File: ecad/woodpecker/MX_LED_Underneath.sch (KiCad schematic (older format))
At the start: 6 parts, among them SW1 Cherry_MX_LED, U1 TLC5973

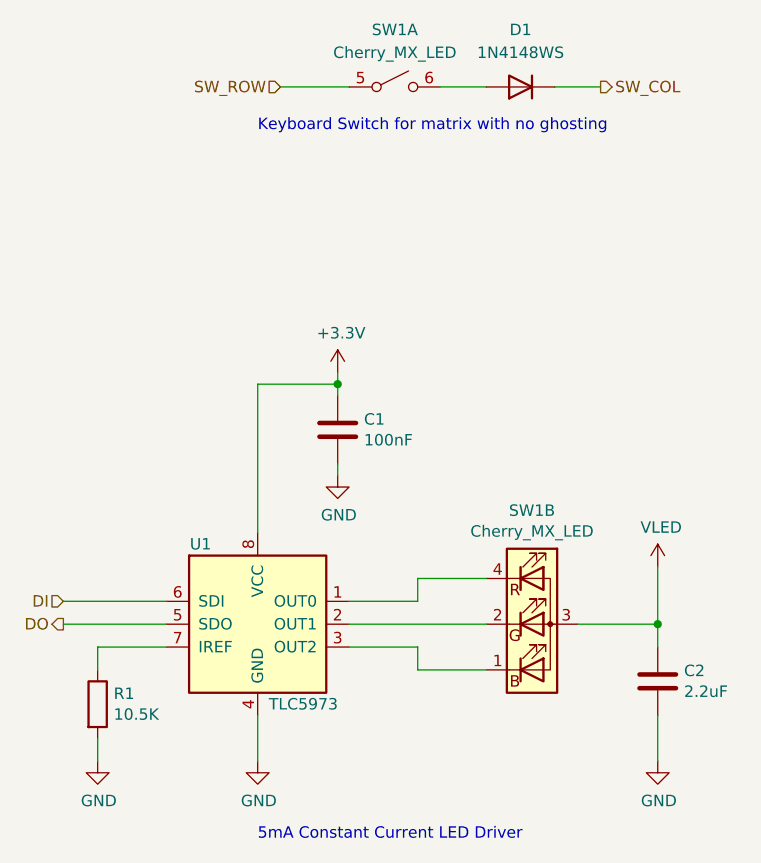
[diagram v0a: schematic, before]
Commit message: Adds bottom section in monolithic design
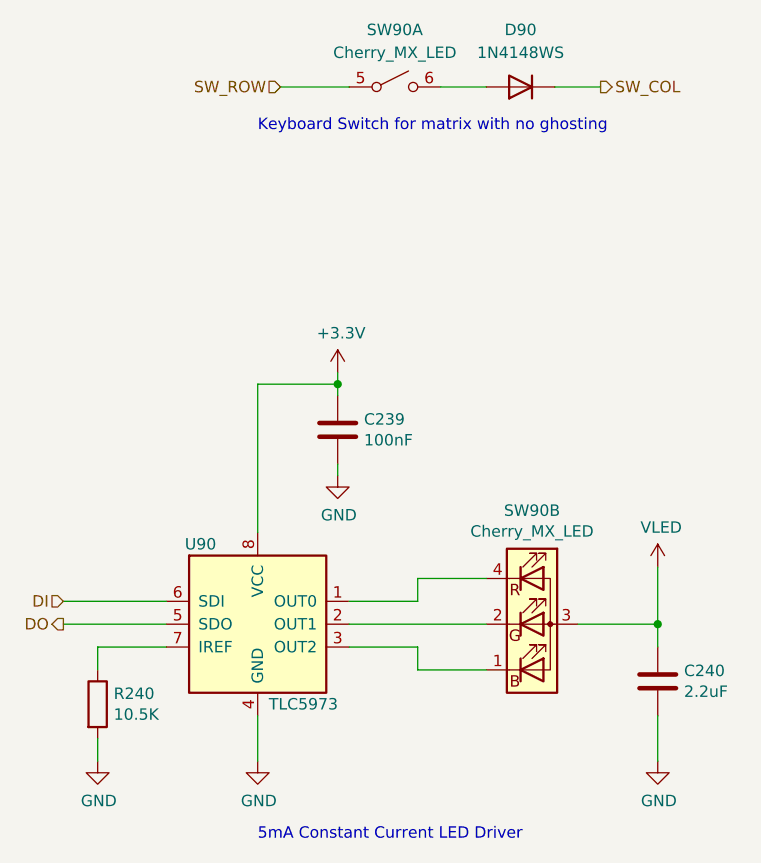
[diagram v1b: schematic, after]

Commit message: Corrects Quadrature encoder debounce circuit on put them on the scan matrix
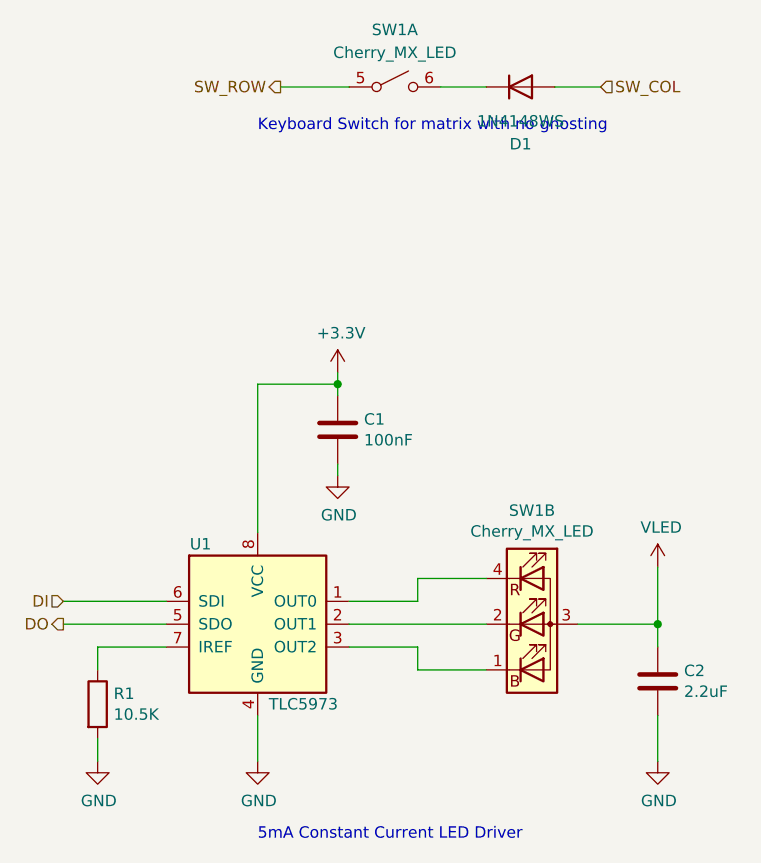
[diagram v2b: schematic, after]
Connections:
- net SW_COL: now also D1.2 (A); no longer D1.1 (K)
- net at SW1.6 (SW_B): now also D1.1 (K); no longer D1.2 (A)
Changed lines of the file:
@@
 $Descr A4 11693 8268
 encoding utf-8
-Sheet 81 97
+Sheet 3 97
 Title ""
 Date ""
@@
 AR Path="/60B694C9/60B3E46F/604B48F1" Ref="SW89"  Part="1"
 AR Path="/60B694C9/60B3E4B2/604B48F1" Ref="SW90"  Part="1"
-F 0 "SW90" H 5700 2950 50  0000 C CNN
+F 0 "SW1" H 5700 2950 50  0000 C CNN
 F 1 "Cherry_MX_LED" H 5700 2850 50  0000 C CNN
 F 2 "woodpecker:SW_Cherry_MX_1.00u_PCB_SMD_LED" H 5700 2700 50  0001 C CNN
@@
 AR Path="/60B694C9/60B3E46F/604B519A" Ref="SW89"  Part="2"
 AR Path="/60B694C9/60B3E4B2/604B519A" Ref="SW90"  Part="2"
-F 0 "SW90" H 6300 5547 50  0000 C CNN
+F 0 "SW1" H 6300 5547 50  0000 C CNN
 F 1 "Cherry_MX_LED" H 6300 5456 50  0000 C CNN
 F 2 "woodpecker:SW_Cherry_MX_1.00u_PCB_SMD_LED" H 6300 5050 50  0001 C CNN
@@
 AR Path="/60B694C9/60B3E46F/604B51B1" Ref="U89"  Part="1"
 AR Path="/60B694C9/60B3E4B2/604B51B1" Ref="U90"  Part="1"
-F 0 "U90" H 4850 5400 50  0000 C CNN
+F 0 "U1" H 4850 5400 50  0000 C CNN
 F 1 "TLC5973" H 5300 4700 50  0000 C CNN
 F 2 "Package_SO:SOIC-8_3.9x4.9mm_P1.27mm" H 5550 5400 50  0001 L CNN
@@
 AR Path="/60B694C9/60B3E46F/604BE188" Ref="C238"  Part="1"
 AR Path="/60B694C9/60B3E4B2/604BE188" Ref="C240"  Part="1"
-F 0 "C240" H 6965 5346 50  0000 L CNN
+F 0 "C2" H 6965 5346 50  0000 L CNN
 F 1 "2.2uF" H 6965 5255 50  0000 L CNN
 F 2 "Capacitor_SMD:C_0805_2012Metric_Pad1.18x1.45mm_HandSolder" H 6888 5150 50  0001 C CNN
@@
 AR Path="/60B694C9/60B3E46F/604BF391" Ref="#PWR0649"  Part="1"
 AR Path="/60B694C9/60B3E4B2/604BF391" Ref="#PWR0655"  Part="1"
-F 0 "#PWR0655" H 6850 5400 50  0001 C CNN
+F 0 "#PWR06" H 6850 5400 50  0001 C CNN
 F 1 "GND" H 6855 5477 50  0000 C CNN
 F 2 "" H 6850 5650 50  0001 C CNN
@@
 AR Path="/60B694C9/60B3E46F/604BFB17" Ref="#PWR0650"  Part="1"
 AR Path="/60B694C9/60B3E4B2/604BFB17" Ref="#PWR0656"  Part="1"
-F 0 "#PWR0656" H 5100 5400 50  0001 C CNN
+F 0 "#PWR02" H 5100 5400 50  0001 C CNN
 F 1 "GND" H 5105 5477 50  0000 C CNN
 F 2 "" H 5100 5650 50  0001 C CNN
@@
 AR Path="/60B694C9/60B3E46F/604C10C7" Ref="#PWR0651"  Part="1"
 AR Path="/60B694C9/60B3E4B2/604C10C7" Ref="#PWR0657"  Part="1"
-F 0 "#PWR0657" H 5450 3800 50  0001 C CNN
+F 0 "#PWR03" H 5450 3800 50  0001 C CNN
 F 1 "+3.3V" H 5465 4123 50  0000 C CNN
 F 2 "" H 5450 3950 50  0001 C CNN
@@
 AR Path="/60B694C9/60B3E46F/604C2DB8" Ref="C237"  Part="1"
 AR Path="/60B694C9/60B3E4B2/604C2DB8" Ref="C239"  Part="1"
-F 0 "C239" H 5565 4246 50  0000 L CNN
+F 0 "C1" H 5565 4246 50  0000 L CNN
 F 1 "100nF" H 5565 4155 50  0000 L CNN
 F 2 "Capacitor_SMD:C_0603_1608Metric_Pad1.08x0.95mm_HandSolder" H 5488 4050 50  0001 C CNN
@@
 AR Path="/60B694C9/60B3E46F/604CD79F" Ref="#PWR0652"  Part="1"
 AR Path="/60B694C9/60B3E4B2/604CD79F" Ref="#PWR0658"  Part="1"
-F 0 "#PWR0658" H 5450 4150 50  0001 C CNN
+F 0 "#PWR04" H 5450 4150 50  0001 C CNN
 F 1 "GND" H 5455 4227 50  0000 C CNN
 F 2 "" H 5450 4400 50  0001 C CNN
@@
 AR Path="/60B694C9/60B3E46F/604CFE96" Ref="R239"  Part="1"
 AR Path="/60B694C9/60B3E4B2/604CFE96" Ref="R240"  Part="1"
-F 0 "R240" H 4470 5446 50  0000 L CNN
+F 0 "R1" H 4470 5446 50  0000 L CNN
 F 1 "10.5K" H 4470 5355 50  0000 L CNN
 F 2 "Resistor_SMD:R_0603_1608Metric_Pad0.98x0.95mm_HandSolder" V 4330 5400 50  0001 C CNN
@@
 AR Path="/60B694C9/60B3E46F/604D1ECE" Ref="#PWR0653"  Part="1"
 AR Path="/60B694C9/60B3E4B2/604D1ECE" Ref="#PWR0659"  Part="1"
-F 0 "#PWR0659" H 4400 5400 50  0001 C CNN
+F 0 "#PWR01" H 4400 5400 50  0001 C CNN
 F 1 "GND" H 4405 5477 50  0000 C CNN
 F 2 "" H 4400 5650 50  0001 C CNN
@@
 Text Notes 5100 2900 0    50   ~ 0
 Keyboard Switch for matrix with no ghosting
-Text HLabel 6600 2700 2    50   Output ~ 0
+Text HLabel 6600 2700 2    50   Input ~ 0
 SW_COL
-Text HLabel 5200 2700 0    50   Input ~ 0
+Text HLabel 5200 2700 0    50   Output ~ 0
 SW_ROW
 Wire Wire Line
@@
 AR Path="/60B694C9/60B3E46F/604B9203" Ref="D89"  Part="1"
 AR Path="/60B694C9/60B3E4B2/604B9203" Ref="D90"  Part="1"
-F 0 "D90" H 6250 2450 50  0000 C CNN
+F 0 "D1" H 6250 2450 50  0000 C CNN
 F 1 "1N4148WS" H 6250 2550 50  0000 C CNN
 F 2 "Diode_SMD:D_SOD-323_HandSoldering" H 6250 2525 50  0001 C CNN
 F 3 "https://www.vishay.com/docs/85751/1n4148ws.pdf" H 6250 2700 50  0001 C CNN
 	1    6250 2700
-	-1   0    0    1
+	1    0    0    -1
 $EndComp
 Wire Wire Line
@@
 AR Path="/60B694C9/60B3E46F/604C33E4" Ref="#PWR0654"  Part="1"
 AR Path="/60B694C9/60B3E4B2/604C33E4" Ref="#PWR0660"  Part="1"
-F 0 "#PWR0660" H 6650 4650 50  0001 C CNN
+F 0 "#PWR05" H 6650 4650 50  0001 C CNN
 F 1 "VLED" H 6865 4973 50  0000 C CNN
 F 2 "" H 6850 4800 50  0001 C CNN
